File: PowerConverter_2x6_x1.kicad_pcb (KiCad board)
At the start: 2 copper layers, 82.5 x 29 mm, 19 parts, among them J1 Conn_01x05, J2 Conn_01x05, J3 Conn_01x05, J4 Conn_01x05, J5 Regulator connector, J6 JST_SH_SM06B-SRSS-TB_1x06-1MP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, J7 Conn_01x04, U1 M24C02-FMN

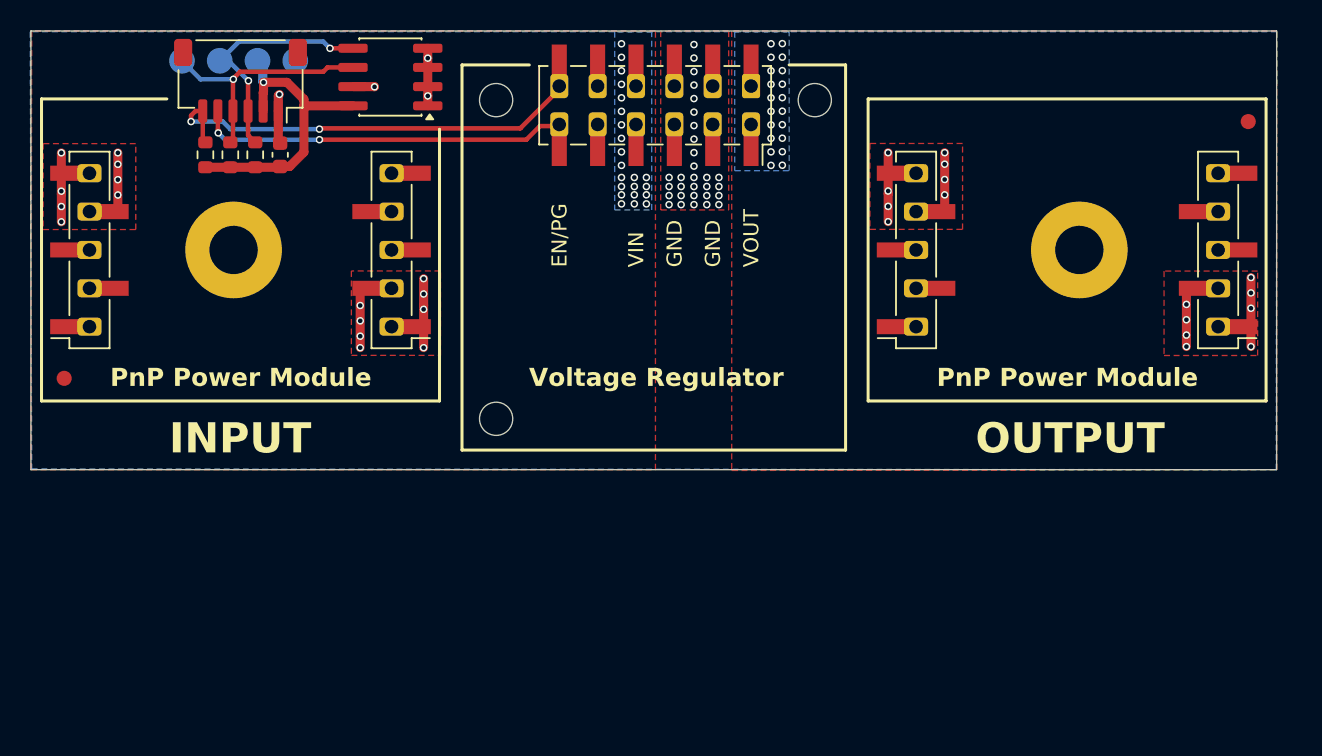
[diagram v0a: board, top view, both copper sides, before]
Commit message: Rotate regulator 90deg to have better connection to VIN and VOUT lines
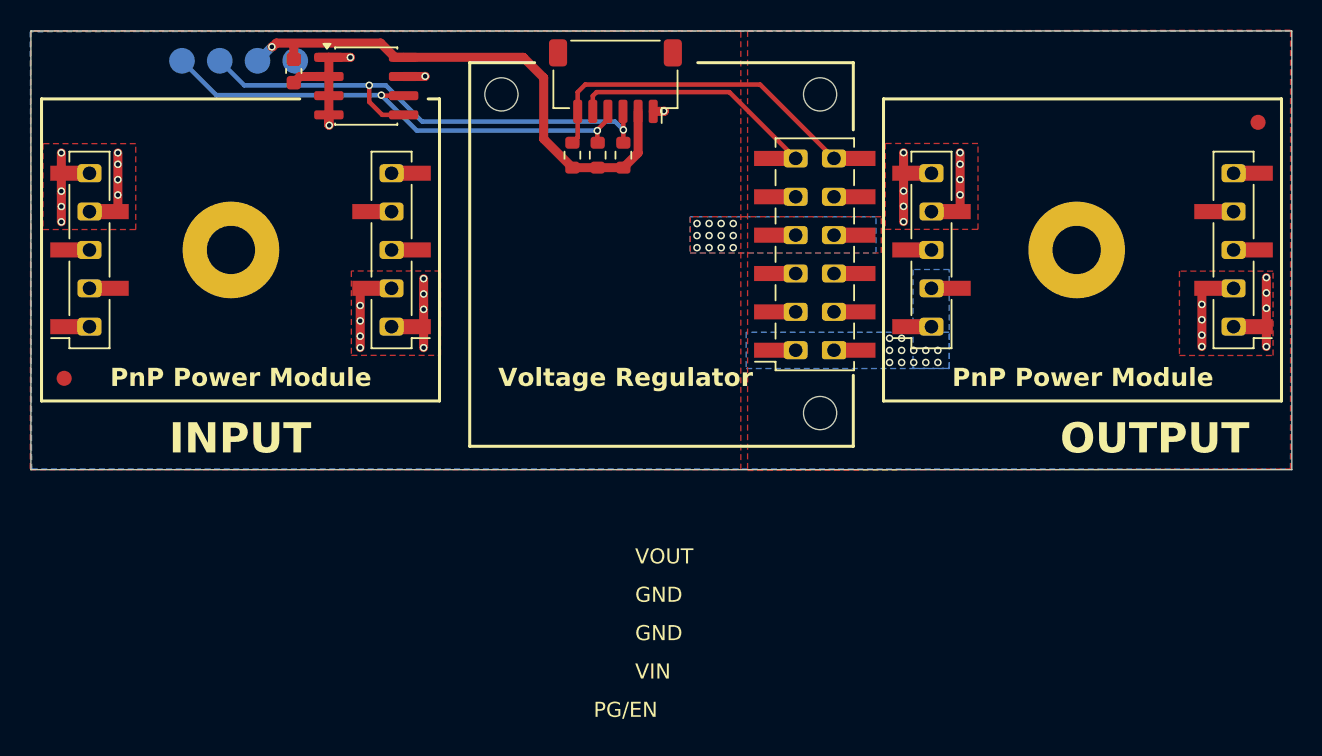
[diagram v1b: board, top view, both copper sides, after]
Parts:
- removed the REF** at (113.1, 119.1)
- removed the REF** at (113.1, 140.2)
- removed the REF** at (134.2, 119.1)
- added REF**: MountingHole_2.2mm_M2, MountingHole:MountingHole_2.2mm_M2, F.Cu at (134.6, 118.8)
- added REF**: MountingHole_2.2mm_M2, MountingHole:MountingHole_2.2mm_M2, F.Cu at (113.5, 118.8)
- added REF**: MountingHole_2.2mm_M2, MountingHole:MountingHole_2.2mm_M2, F.Cu at (134.6, 139.8)
- moved J6 24.8 mm to (121.0, 117.9)
- moved R1 24.4 mm to (121.5, 122.8)
- moved R2 24.3 mm to (119.8, 122.8)
- moved R3 24.3 mm to (118.2, 122.8)
- moved J5 14.5 mm to (134.2, 129.3), turned to 180 degrees
- moved C1 5.62 mm to (99.7, 117.2), turned to -90 degrees
- moved U1 1.71 mm to (104.5, 118.2), turned to 0 degrees
- moved J4 1.02 mm to (161.9, 129.1)
- moved J3 1.02 mm to (141.9, 129.1)
- moved REF** 0.65 mm to (163.6, 120.6)
- moved REF** 0.17 mm to (95.5, 129.1)
- moved REF** 0.17 mm to (151.5, 129.1)
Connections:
- J1 pad 3: (no net) -> unconnected-(J1-Pin_3-Pad3)
- J2 pad 3: (no net) -> unconnected-(J2-Pin_3-Pad3)_1
- J3 pad 3: (no net) -> unconnected-(J3-Pin_3-Pad3)_1
- J4 pad 3: (no net) -> unconnected-(J4-Pin_3-Pad3)
- J5 pad 10: (no net) -> unconnected-(J5-Pin_10-Pad10)_1
- J5 pad 9: (no net) -> unconnected-(J5-Pin_9-Pad9)
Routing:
- net SDA: track 16.3 -> 35.0 mm
- net SCL: track 16.5 -> 33.3 mm, vias 1 -> 2
- net VCC: track 20.9 -> 36.5 mm
- net EN/INT1: track 24.6 -> 16.4 mm, vias 2 -> 0
- net PG/INT2: track 29.7 -> 22.7 mm, vias 2 -> 0
- net GND: track 46.8 -> 50.2 mm, vias 66 -> 36
- net VIN: track 0.76 -> 0.00 mm, vias 22 -> 12
- net VOUT: track 1.11 -> 0.35 mm, vias 20 -> 12
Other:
- board size 82.5 x 29 mm -> 83.5 x 29 mm
- board text added: "PG/EN"
- board text added: "Plug-n-Play Power Converter 1x6 x1"
- board text removed: "EN/PG"
- board text removed: "Plug-n-Play Power Converter 2x6 x1"
